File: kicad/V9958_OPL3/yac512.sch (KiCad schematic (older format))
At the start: 1 part, among them U9 YAC512

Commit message: update
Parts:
- U9: footprint (none) -> Housings_SOIC:SOIC-16_3.9x9.9mm_Pitch1.27mm
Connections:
- net DIN: now reaches U9.4 (DIN)
- net CLK: now reaches U9.5 (CLK)
- net SMP2: now reaches U9.7 (SMP2)
- net SMP1: now reaches U9.8 (SMP1)
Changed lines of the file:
@@
 F 0 "U9" H 3650 2600 60  0000 C CNN
 F 1 "YAC512" H 3650 2500 60  0000 C CNN
-F 2 "" H 3650 2550 60  0000 C CNN
+F 2 "Housings_SOIC:SOIC-16_3.9x9.9mm_Pitch1.27mm" H 3650 2550 60  0001 C CNN
 F 3 "" H 3650 2550 60  0000 C CNN
 	1    3650 2550
 	1    0    0    -1
 $EndComp
+Text HLabel 2700 2500 0    60   Input ~ 0
+DIN
+Wire Wire Line
+	2700 2500 2850 2500
+Text HLabel 2700 2600 0    60   Input ~ 0
+CLK
+Wire Wire Line
+	2700 2600 2850 2600
+Text HLabel 2700 2900 0    60   Input ~ 0
+SMP1
+Text HLabel 2700 2800 0    60   Input ~ 0
+SMP2
+Wire Wire Line
+	2700 2800 2850 2800
+Wire Wire Line
+	2700 2900 2850 2900
 $EndSCHEMATC

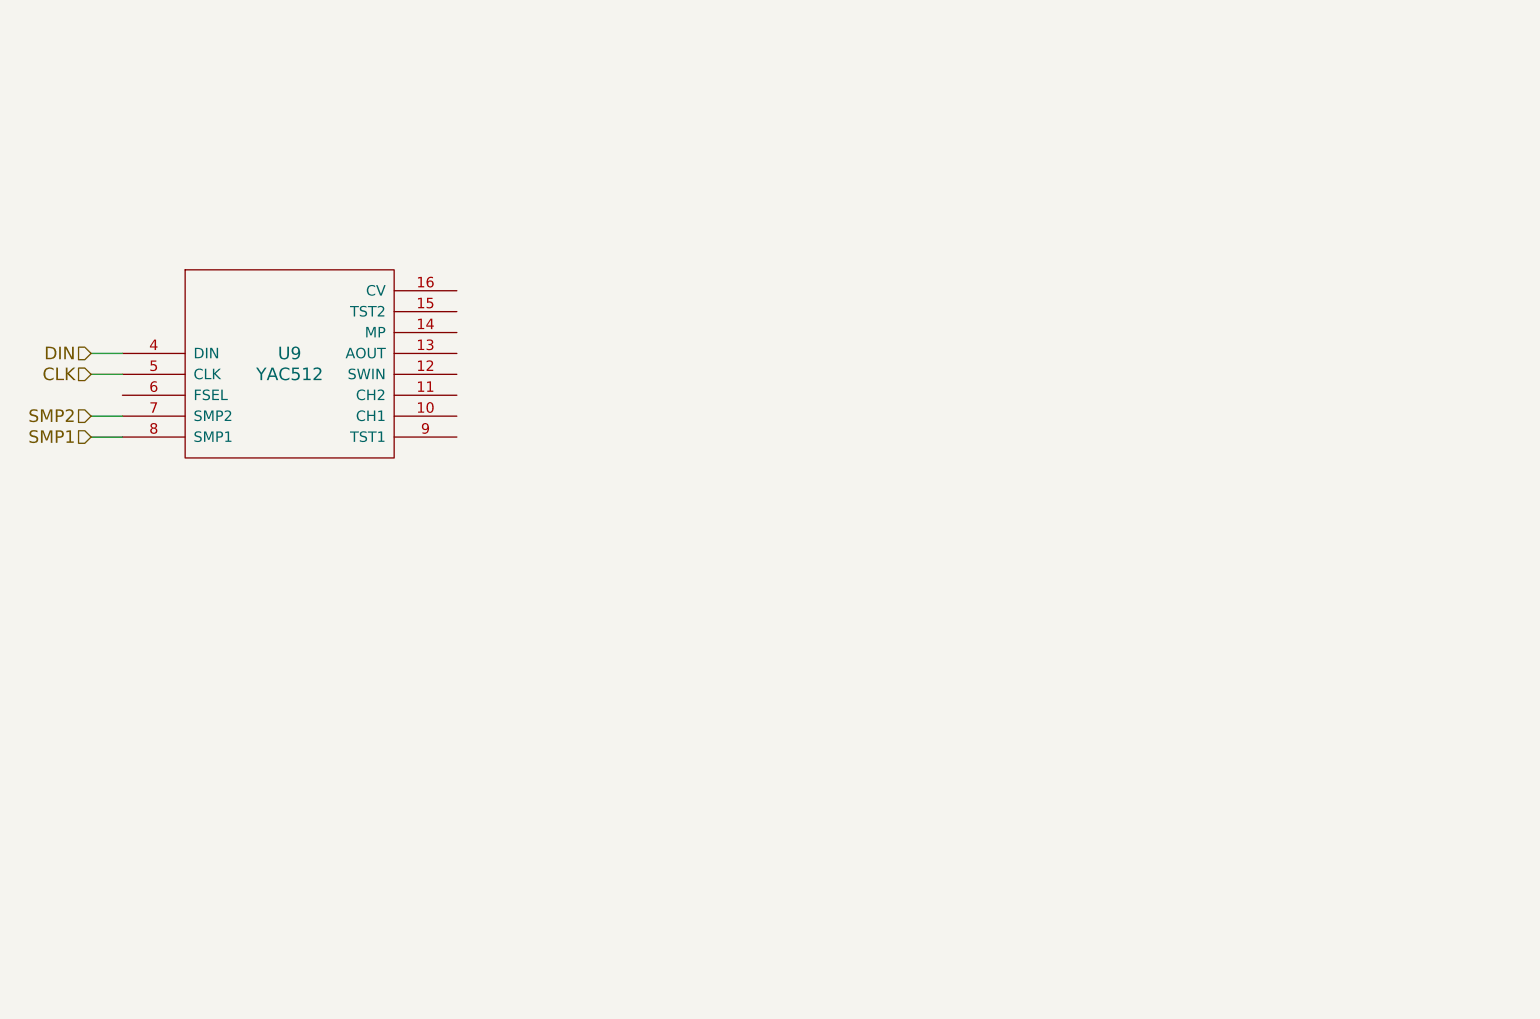
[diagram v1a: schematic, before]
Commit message: OP output stage
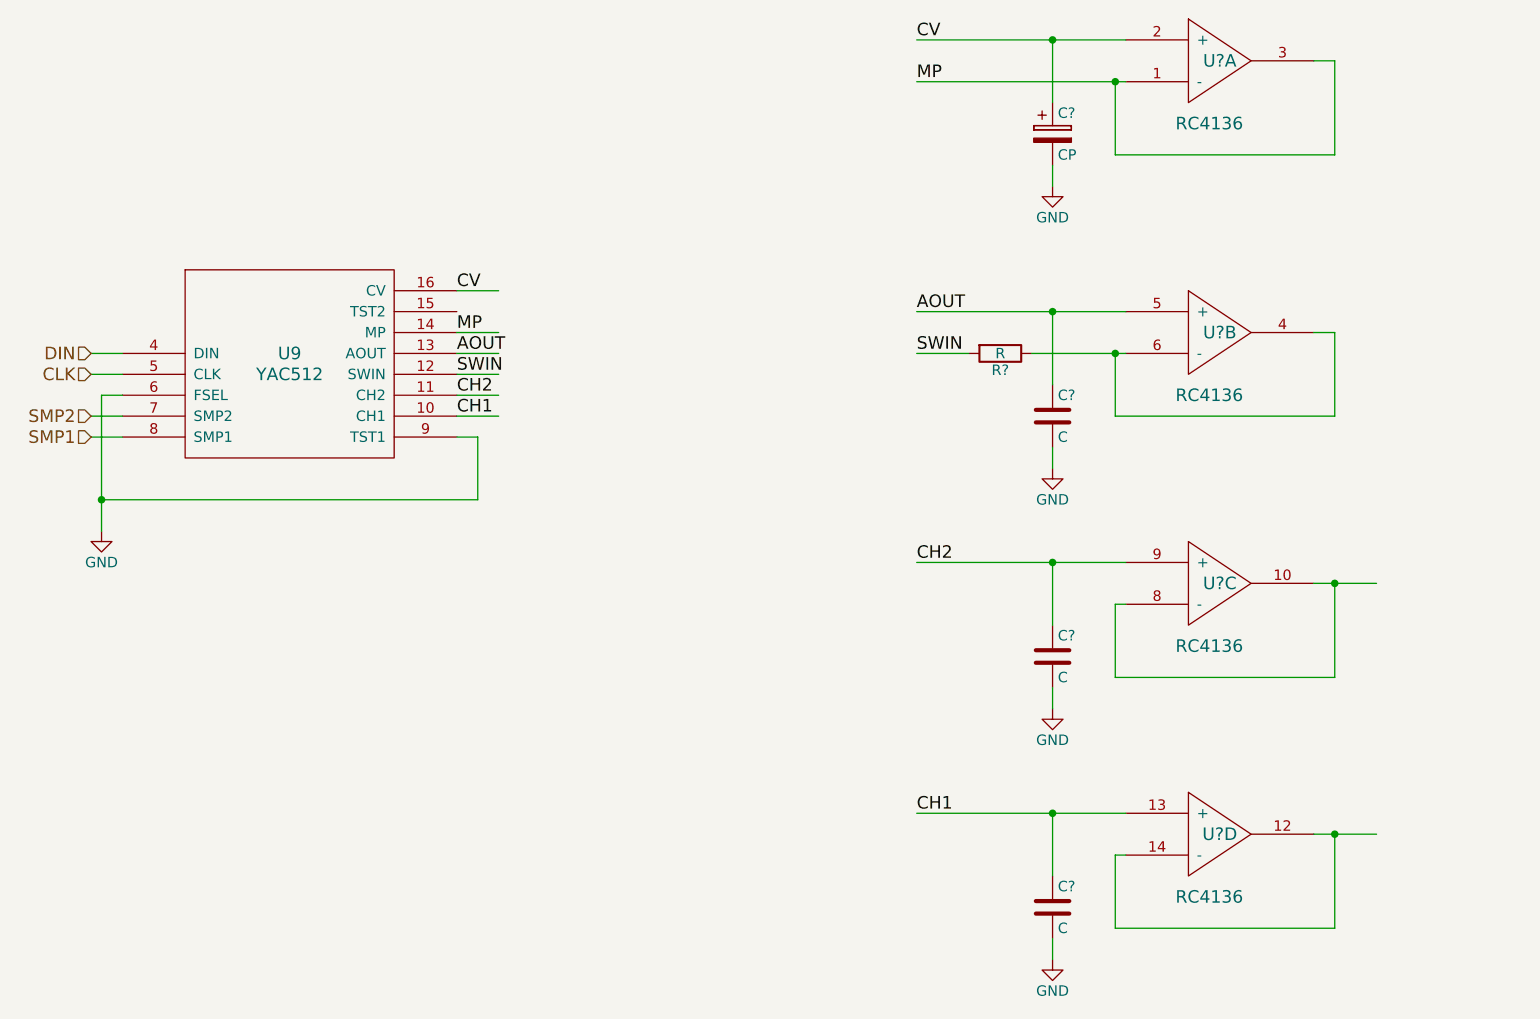
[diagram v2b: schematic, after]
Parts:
- added C?: CP, symbol CP
- added C? (x3): C, symbol C
- added R?: R, symbol R
- added U? (x4): RC4136, symbol RC4136
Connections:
- net labels added: AOUT, CH1, CH2, CV, GND, MP, SWIN
- wire segments 4 -> 48

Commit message: dsub9-connector for RGB, pinout like 1084S D2
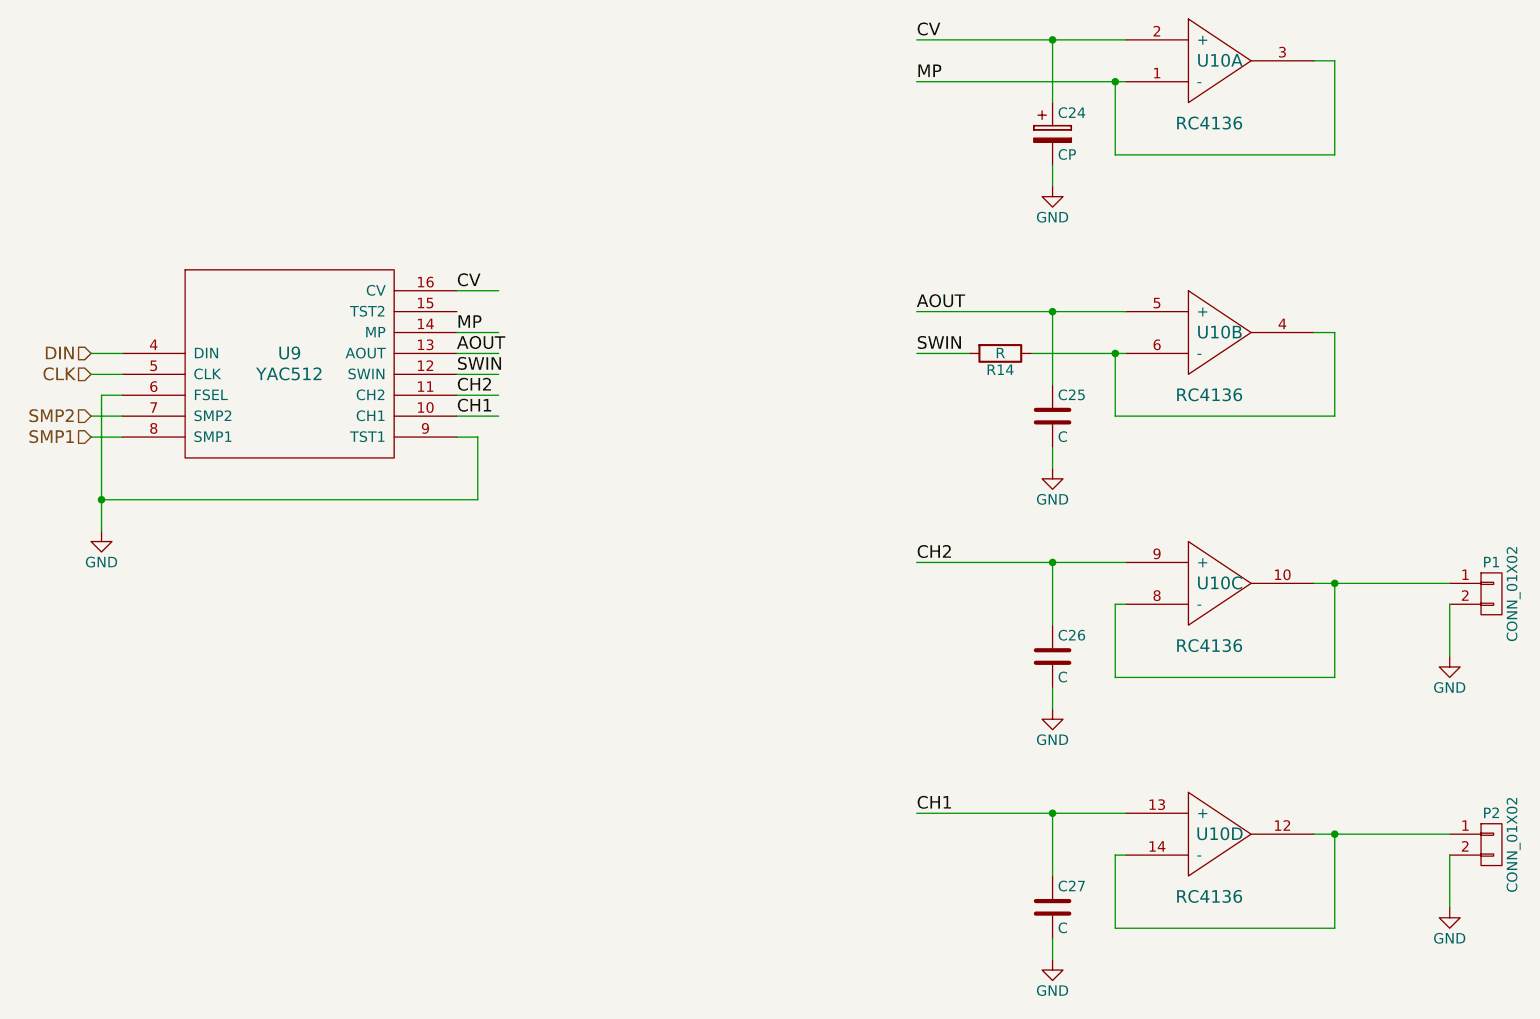
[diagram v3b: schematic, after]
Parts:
- added P1, P2: CONN_01X02, Pin_Headers:Pin_Header_Straight_1x02, symbol CONN_01X02
- C24: renamed from C?; footprint (none) -> Capacitors_ThroughHole:C_Radial_D6.3_L11.2_P2.5
- C25, C26, C27: renamed from C?; footprint (none) -> Capacitors_ThroughHole:C_Disc_D3_P2.5
- R14: renamed from R?; footprint (none) -> Discret:R3
- U10: renamed from U?; footprint (none) -> Housings_DIP:DIP-14_W7.62mm_LongPads
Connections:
- wire segments 48 -> 50
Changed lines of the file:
@@
 LIBS:yamaha_opl
 LIBS:rc4136
+LIBS:audio
 LIBS:v9958-cache
 EELAYER 25 0
@@
 	2700 2900 2850 2900
 $Comp
-L GND #PWR?
+L GND #PWR040
 U 1 1 5B0AC7A9
 P 2750 3350
-F 0 "#PWR?" H 2750 3100 50  0001 C CNN
+F 0 "#PWR040" H 2750 3100 50  0001 C CNN
 F 1 "GND" H 2750 3200 50  0000 C CNN
 F 2 "" H 2750 3350 50  0000 C CNN
@@
 Connection ~ 2750 3200
 $Comp
-L RC4136 U?
+L RC4136 U10
 U 1 1 5B0AC7DC
 P 8100 1100
-F 0 "U?" H 8100 1100 60  0000 C CNN
+F 0 "U10" H 8100 1100 60  0000 C CNN
 F 1 "RC4136" H 8050 800 60  0000 C CNN
-F 2 "" H 8100 1100 60  0000 C CNN
+F 2 "Housings_DIP:DIP-14_W7.62mm_LongPads" H 8100 1100 60  0001 C CNN
 F 3 "" H 8100 1100 60  0000 C CNN
 	1    8100 1100
@@
 	6650 1200 7650 1200
 $Comp
-L CP C?
+L CP C24
 U 1 1 5B0AC887
 P 7300 1450
-F 0 "C?" H 7325 1550 50  0000 L CNN
+F 0 "C24" H 7325 1550 50  0000 L CNN
 F 1 "CP" H 7325 1350 50  0000 L CNN
-F 2 "" H 7338 1300 50  0000 C CNN
+F 2 "Capacitors_ThroughHole:C_Radial_D6.3_L11.2_P2.5" H 7338 1300 50  0001 C CNN
 F 3 "" H 7300 1450 50  0000 C CNN
 	1    7300 1450
@@
 Connection ~ 7300 1000
 $Comp
-L GND #PWR?
+L GND #PWR041
 U 1 1 5B0AC937
 P 7300 1700
-F 0 "#PWR?" H 7300 1450 50  0001 C CNN
+F 0 "#PWR041" H 7300 1450 50  0001 C CNN
 F 1 "GND" H 7300 1550 50  0000 C CNN
 F 2 "" H 7300 1700 50  0000 C CNN
@@
 Connection ~ 7600 1200
 $Comp
-L RC4136 U?
+L RC4136 U10
 U 2 1 5B0AC9F5
 P 8100 2400
-F 0 "U?" H 8100 2400 60  0000 C CNN
+F 0 "U10" H 8100 2400 60  0000 C CNN
 F 1 "RC4136" H 8050 2100 60  0000 C CNN
-F 2 "" H 8100 2400 60  0000 C CNN
+F 2 "Housings_DIP:DIP-14_W7.62mm_LongPads" H 8100 2400 60  0001 C CNN
 F 3 "" H 8100 2400 60  0000 C CNN
 	2    8100 2400
@@
 	7650 2300 6650 2300
 $Comp
-L R R?
+L R R14
 U 1 1 5B0ACE42
 P 7050 2500
-F 0 "R?" V 7130 2500 50  0000 C CNN
+F 0 "R14" V 7130 2500 50  0000 C CNN
 F 1 "R" V 7050 2500 50  0000 C CNN
-F 2 "" V 6980 2500 50  0000 C CNN
+F 2 "Discret:R3" V 6980 2500 50  0001 C CNN
 F 3 "" H 7050 2500 50  0000 C CNN
 	1    7050 2500
@@
 	7200 2500 7650 2500
 $Comp
-L C C?
+L C C25
 U 1 1 5B0ACEEC
 P 7300 2800
-F 0 "C?" H 7325 2900 50  0000 L CNN
+F 0 "C25" H 7325 2900 50  0000 L CNN
 F 1 "C" H 7325 2700 50  0000 L CNN
-F 2 "" H 7338 2650 50  0000 C CNN
+F 2 "Capacitors_ThroughHole:C_Disc_D3_P2.5" H 7338 2650 50  0001 C CNN
 F 3 "" H 7300 2800 50  0000 C CNN
 	1    7300 2800
@@
 Connection ~ 7300 2300
 $Comp
-L GND #PWR?
+L GND #PWR042
 U 1 1 5B0ACF5E
 P 7300 3050
-F 0 "#PWR?" H 7300 2800 50  0001 C CNN
+F 0 "#PWR042" H 7300 2800 50  0001 C CNN
 F 1 "GND" H 7300 2900 50  0000 C CNN
 F 2 "" H 7300 3050 50  0000 C CNN
@@
 SWIN
 $Comp
-L RC4136 U?
+L RC4136 U10
 U 3 1 5B0AD175
 P 8100 3600
-F 0 "U?" H 8100 3600 60  0000 C CNN
+F 0 "U10" H 8100 3600 60  0000 C CNN
 F 1 "RC4136" H 8050 3300 60  0000 C CNN
-F 2 "" H 8100 3600 60  0000 C CNN
+F 2 "Housings_DIP:DIP-14_W7.62mm_LongPads" H 8100 3600 60  0001 C CNN
 F 3 "" H 8100 3600 60  0000 C CNN
 	3    8100 3600
@@
 Connection ~ 7300 3500
 $Comp
-L GND #PWR?
+L GND #PWR043
 U 1 1 5B0AD185
 P 7300 4200
-F 0 "#PWR?" H 7300 3950 50  0001 C CNN
+F 0 "#PWR043" H 7300 3950 50  0001 C CNN
 F 1 "GND" H 7300 4050 50  0000 C CNN
 F 2 "" H 7300 4200 50  0000 C CNN
@@
 	7300 4100 7300 4200
 Wire Wire Line
-	8550 3600 8850 3600
+	8550 3600 9200 3600
 Wire Wire Line
 	8650 3600 8650 4050
@@
 	7600 3700 7650 3700
 $Comp
-L C C?
+L C C26
 U 1 1 5B0AD26F
 P 7300 3950
-F 0 "C?" H 7325 4050 50  0000 L CNN
+F 0 "C26" H 7325 4050 50  0000 L CNN
 F 1 "C" H 7325 3850 50  0000 L CNN
-F 2 "" H 7338 3800 50  0000 C CNN
+F 2 "Capacitors_ThroughHole:C_Disc_D3_P2.5" H 7338 3800 50  0001 C CNN
 F 3 "" H 7300 3950 50  0000 C CNN
 	1    7300 3950
@@
 Connection ~ 7600 2500
 $Comp
-L RC4136 U?
+L RC4136 U10
 U 4 1 5B0AD4B5
 P 8100 4800
-F 0 "U?" H 8100 4800 60  0000 C CNN
+F 0 "U10" H 8100 4800 60  0000 C CNN
 F 1 "RC4136" H 8050 4500 60  0000 C CNN
-F 2 "" H 8100 4800 60  0000 C CNN
+F 2 "Housings_DIP:DIP-14_W7.62mm_LongPads" H 8100 4800 60  0001 C CNN
 F 3 "" H 8100 4800 60  0000 C CNN
 	4    8100 4800
@@
 Connection ~ 7300 4700
 $Comp
-L GND #PWR?
+L GND #PWR044
 U 1 1 5B0AD4BE
 P 7300 5400
-F 0 "#PWR?" H 7300 5150 50  0001 C CNN
+F 0 "#PWR044" H 7300 5150 50  0001 C CNN
 F 1 "GND" H 7300 5250 50  0000 C CNN
 F 2 "" H 7300 5400 50  0000 C CNN
@@
 	7300 5300 7300 5400
 Wire Wire Line
-	8550 4800 8850 4800
+	8550 4800 9200 4800
 Wire Wire Line
 	8650 4800 8650 5250
@@
 	7600 4900 7650 4900
 $Comp
-L C C?
+L C C27
 U 1 1 5B0AD4CB
 P 7300 5150
-F 0 "C?" H 7325 5250 50  0000 L CNN
+F 0 "C27" H 7325 5250 50  0000 L CNN
 F 1 "C" H 7325 5050 50  0000 L CNN
-F 2 "" H 7338 5000 50  0000 C CNN
+F 2 "Capacitors_ThroughHole:C_Disc_D3_P2.5" H 7338 5000 50  0001 C CNN
 F 3 "" H 7300 5150 50  0000 C CNN
 	1    7300 5150
@@
 $EndComp
 Connection ~ 8650 4800
+$Comp
+L CONN_01X02 P1
+U 1 1 5B2FE75D
+P 9400 3650
+F 0 "P1" H 9400 3800 50  0000 C CNN
+F 1 "CONN_01X02" V 9500 3650 50  0000 C CNN
+F 2 "Pin_Headers:Pin_Header_Straight_1x02" H 9400 3650 50  0001 C CNN
+F 3 "" H 9400 3650 50  0000 C CNN
+	1    9400 3650
+	1    0    0    -1
+$EndComp
+$Comp
+L CONN_01X02 P2
+U 1 1 5B2FE82D
+P 9400 4850
+F 0 "P2" H 9400 5000 50  0000 C CNN
+F 1 "CONN_01X02" V 9500 4850 50  0000 C CNN
+F 2 "Pin_Headers:Pin_Header_Straight_1x02" H 9400 4850 50  0001 C CNN
+F 3 "" H 9400 4850 50  0000 C CNN
+	1    9400 4850
+	1    0    0    -1
+$EndComp
+$Comp
+L GND #PWR045
+U 1 1 5B2FE953
+P 9200 3950
+F 0 "#PWR045" H 9200 3700 50  0001 C CNN
+F 1 "GND" H 9200 3800 50  0000 C CNN
+F 2 "" H 9200 3950 50  0000 C CNN
+F 3 "" H 9200 3950 50  0000 C CNN
+	1    9200 3950
+	1    0    0    -1
+$EndComp
+$Comp
+L GND #PWR046
+U 1 1 5B2FE982
+P 9200 5150
+F 0 "#PWR046" H 9200 4900 50  0001 C CNN
+F 1 "GND" H 9200 5000 50  0000 C CNN
+F 2 "" H 9200 5150 50  0000 C CNN
+F 3 "" H 9200 5150 50  0000 C CNN
+	1    9200 5150
+	1    0    0    -1
+$EndComp
+Wire Wire Line
+	9200 3700 9200 3950
+Wire Wire Line
+	9200 4900 9200 5150
 $EndSCHEMATC

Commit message: resistor and capacitor values audio analog section
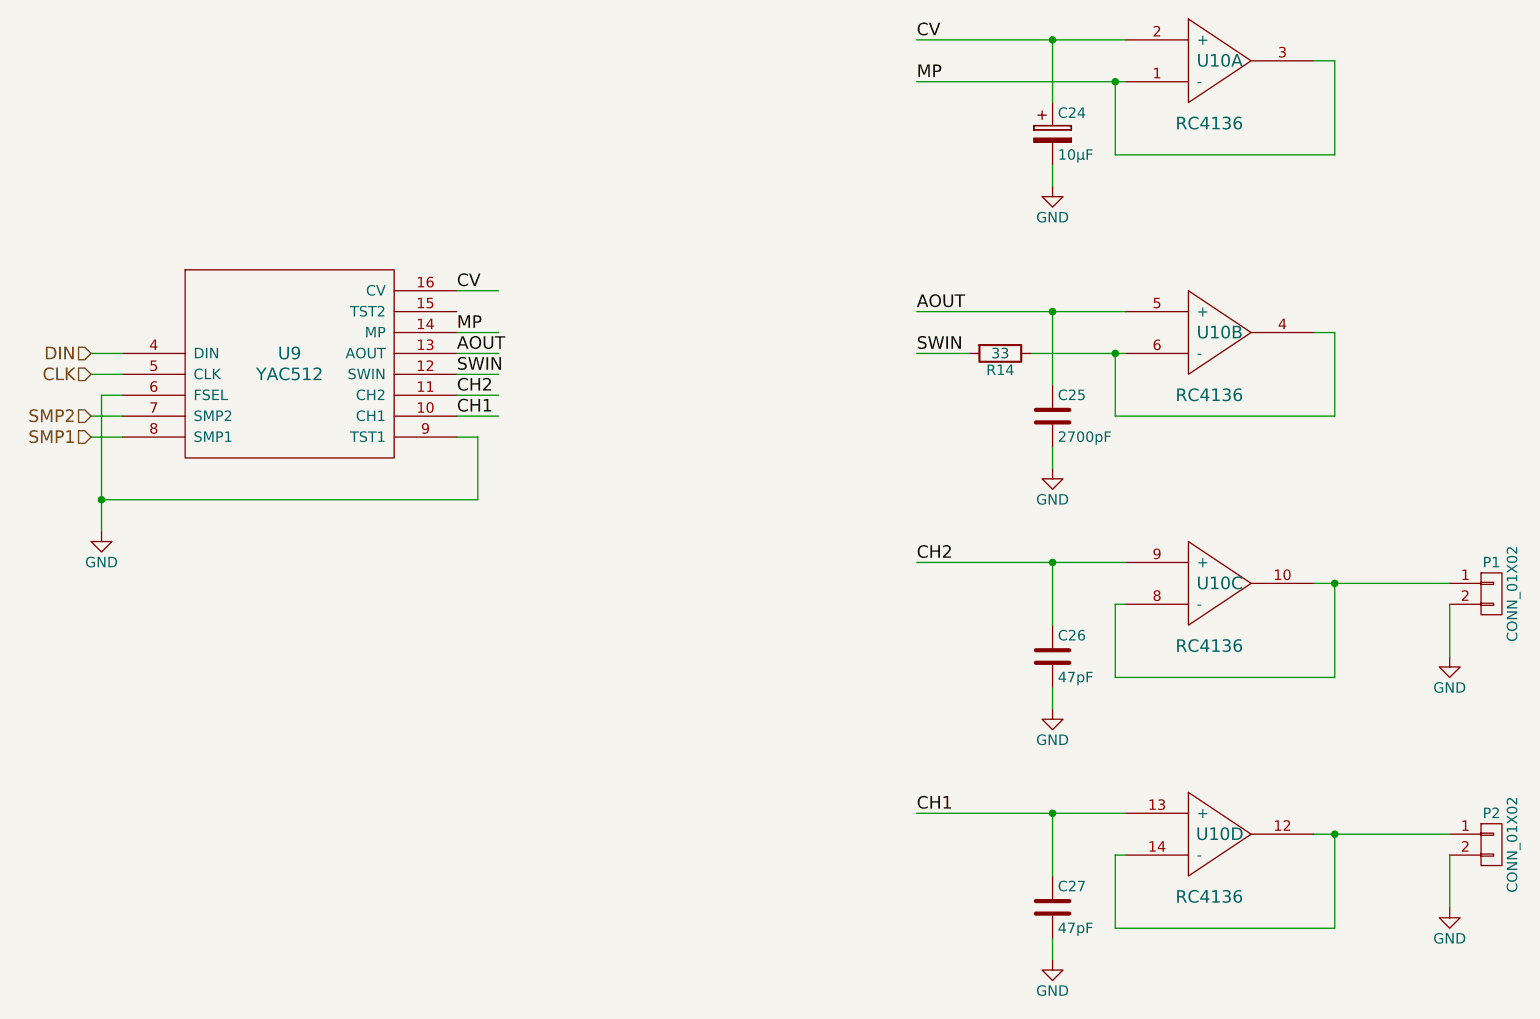
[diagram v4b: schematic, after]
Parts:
- C24: value CP -> 10µF
- C25: value C -> 2700pF
- C26, C27: value C -> 47pF
- R14: value R -> 33
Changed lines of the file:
@@
 EESchema Schematic File Version 2
-LIBS:power
-LIBS:device
-LIBS:transistors
-LIBS:conn
-LIBS:linear
-LIBS:74xx
-LIBS:contrib
 LIBS:tms99xx
 LIBS:dram
@@
 LIBS:yamaha_opl
 LIBS:rc4136
-LIBS:audio
 LIBS:v9958-cache
 EELAYER 25 0
@@
 P 7300 1450
 F 0 "C24" H 7325 1550 50  0000 L CNN
-F 1 "CP" H 7325 1350 50  0000 L CNN
+F 1 "10µF" H 7325 1350 50  0000 L CNN
 F 2 "Capacitors_ThroughHole:C_Radial_D6.3_L11.2_P2.5" H 7338 1300 50  0001 C CNN
 F 3 "" H 7300 1450 50  0000 C CNN
@@
 P 7050 2500
 F 0 "R14" V 7130 2500 50  0000 C CNN
-F 1 "R" V 7050 2500 50  0000 C CNN
+F 1 "33" V 7050 2500 50  0000 C CNN
 F 2 "Discret:R3" V 6980 2500 50  0001 C CNN
 F 3 "" H 7050 2500 50  0000 C CNN
@@
 P 7300 2800
 F 0 "C25" H 7325 2900 50  0000 L CNN
-F 1 "C" H 7325 2700 50  0000 L CNN
+F 1 "2700pF" H 7325 2700 50  0000 L CNN
 F 2 "Capacitors_ThroughHole:C_Disc_D3_P2.5" H 7338 2650 50  0001 C CNN
 F 3 "" H 7300 2800 50  0000 C CNN
@@
 P 7300 3950
 F 0 "C26" H 7325 4050 50  0000 L CNN
-F 1 "C" H 7325 3850 50  0000 L CNN
+F 1 "47pF" H 7325 3850 50  0000 L CNN
 F 2 "Capacitors_ThroughHole:C_Disc_D3_P2.5" H 7338 3800 50  0001 C CNN
 F 3 "" H 7300 3950 50  0000 C CNN
@@
 P 7300 5150
 F 0 "C27" H 7325 5250 50  0000 L CNN
-F 1 "C" H 7325 5050 50  0000 L CNN
+F 1 "47pF" H 7325 5050 50  0000 L CNN
 F 2 "Capacitors_ThroughHole:C_Disc_D3_P2.5" H 7338 5000 50  0001 C CNN
 F 3 "" H 7300 5150 50  0000 C CNN
